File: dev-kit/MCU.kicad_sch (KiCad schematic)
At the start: 34 parts, among them IC107 USBLC6-2P6, IC302 FAN5622SX, IC303 MX25U51245GZ4I00, IC305 NTS0104GU12, M301 NORA-B106, X103 Device, X104 DEBUG, X207 Power, X208 Power, X209 LED Power, X210 Touch Power, X211 IO Power, X302 Display

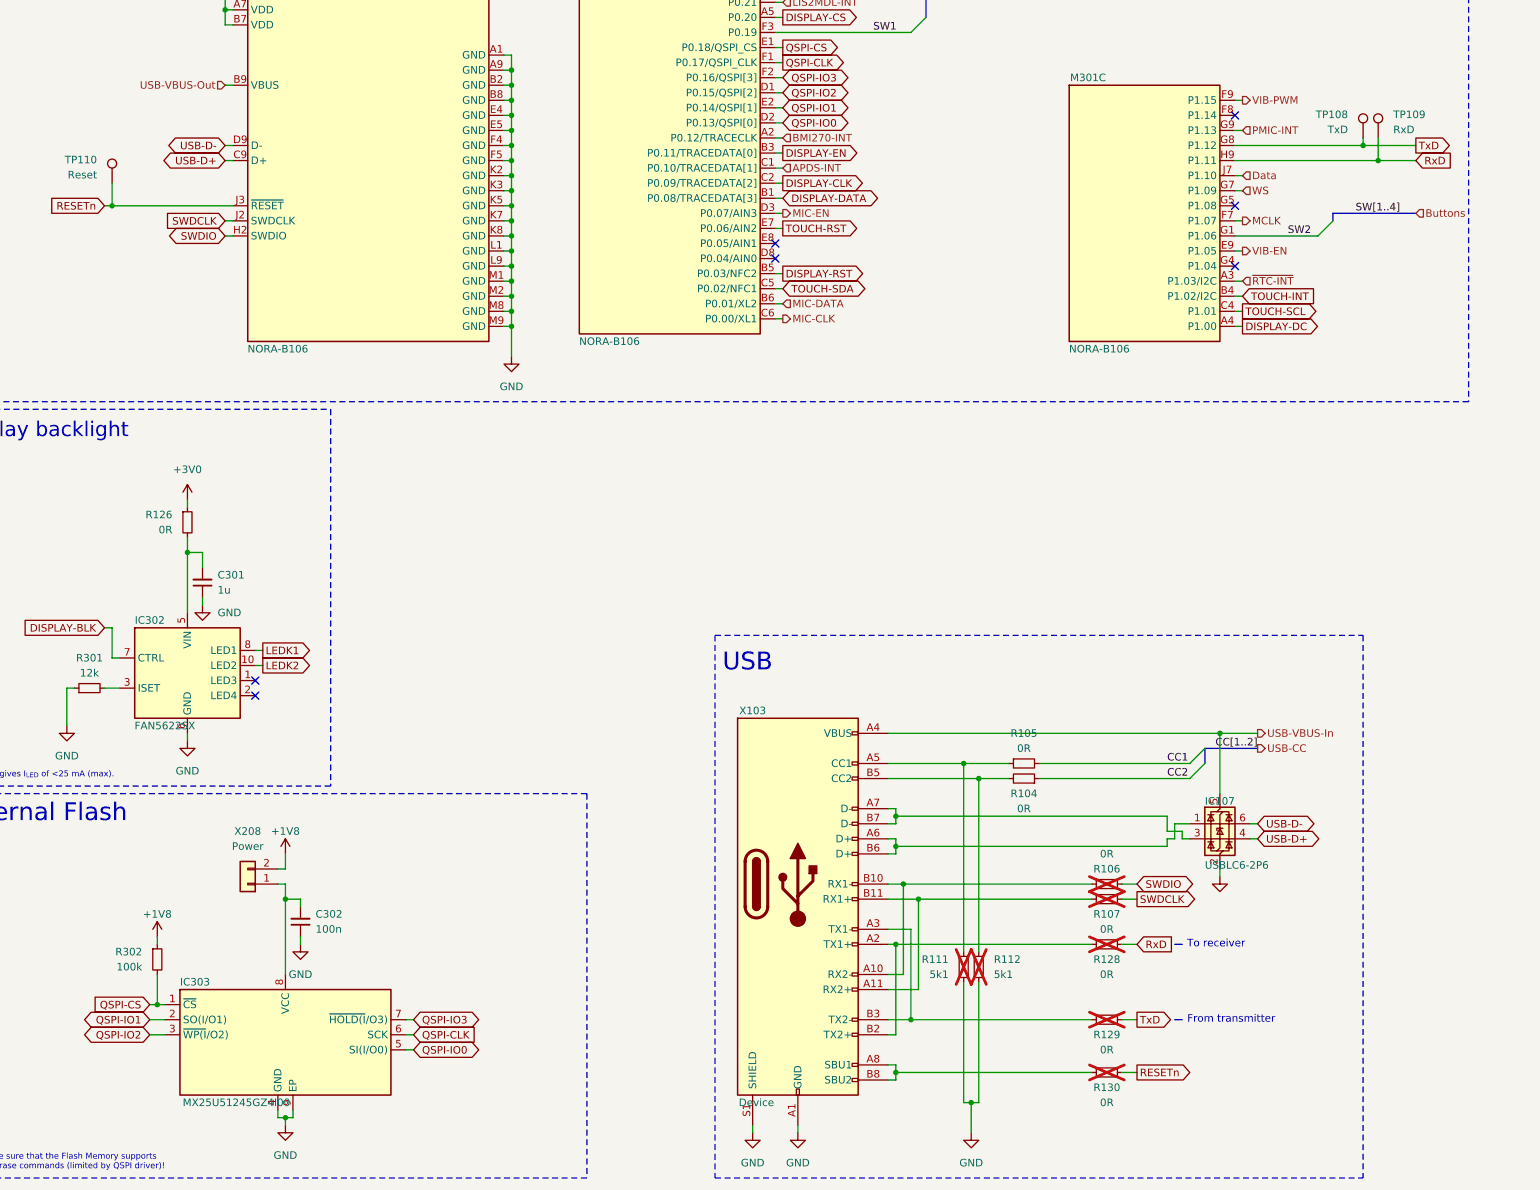
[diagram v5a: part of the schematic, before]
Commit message: PCB: Tweak silkscreen and headers.
- Added silkscreen labels to headers.
- Added function text to buttons.
- Made PCB 5mm wider (left) to make space for display (not sticking out of PCB) and allow more centered
buttons placement.
- Add header for UART pins (good in case we don't have a working dock built) (no mount).
- Changed from TP to header for VBAT for alternative way to connect battery (no mount).
- Added website url on silkscreen.
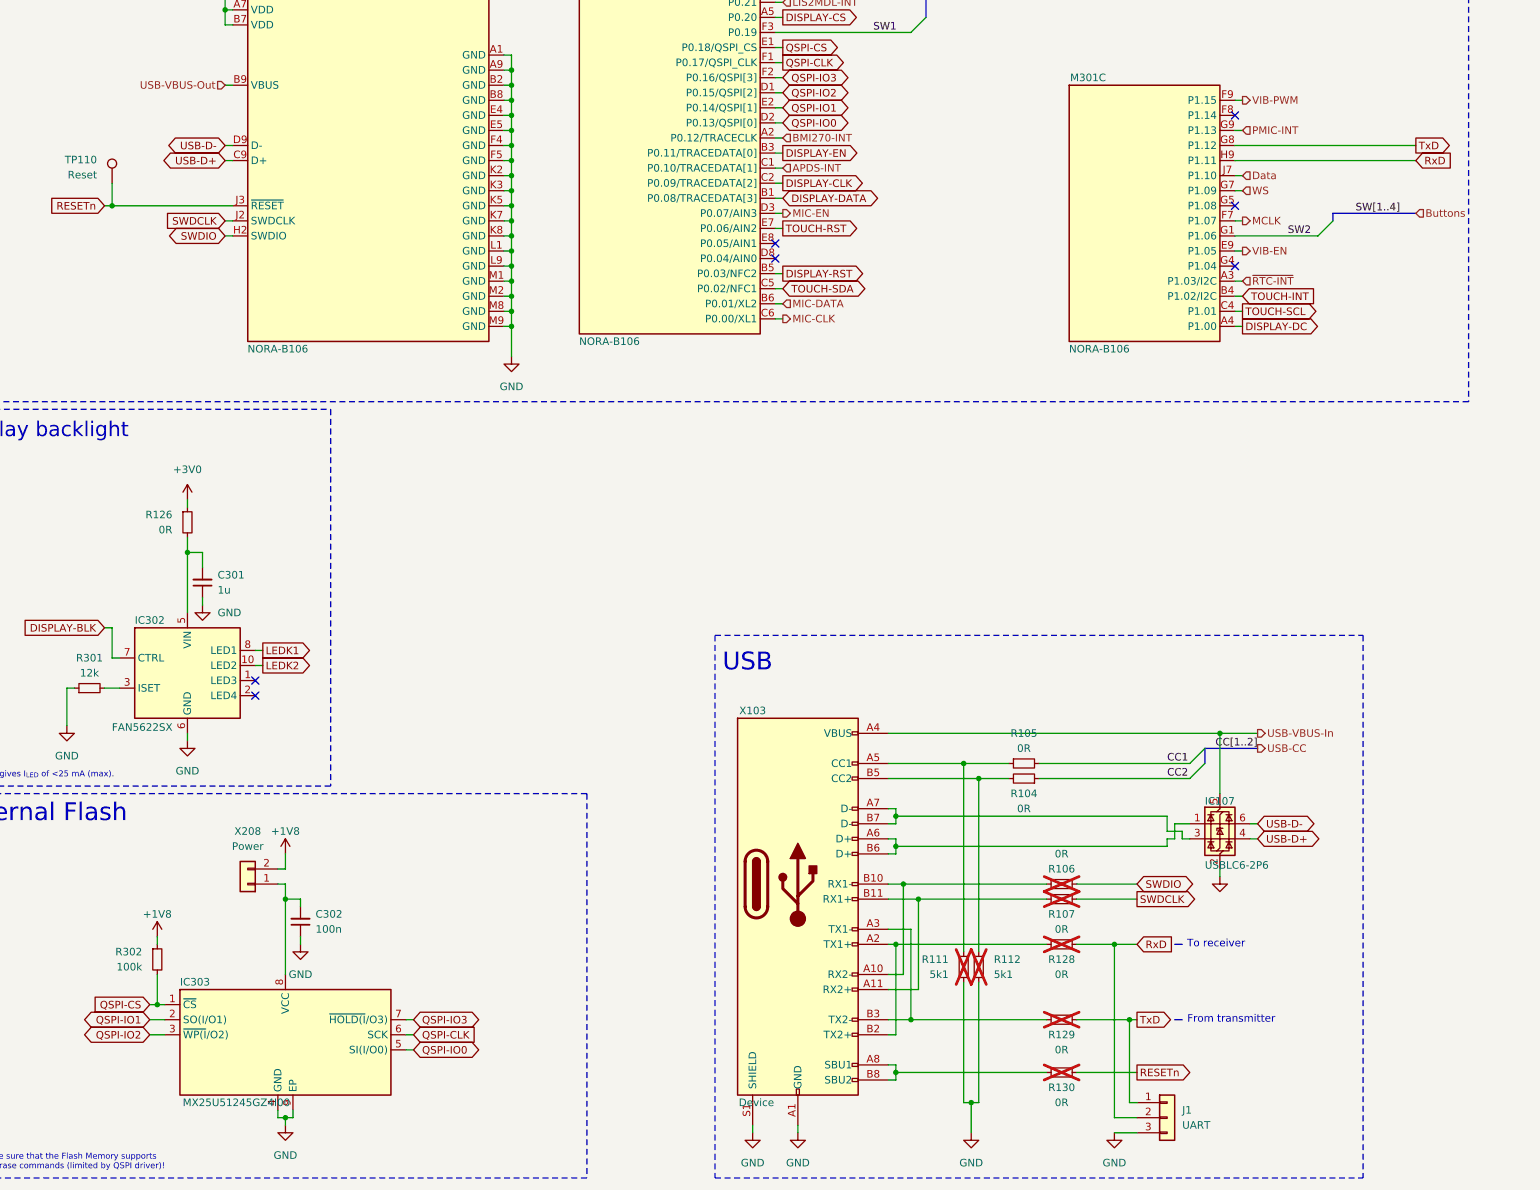
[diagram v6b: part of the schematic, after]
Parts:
- removed TP108: TxD, TestPoint:TestPoint_Pad_D1.0mm, symbol Connector:TestPoint
- removed TP109: RxD, TestPoint:TestPoint_Pad_D1.0mm, symbol Connector:TestPoint
- added J1: UART, Connector_PinHeader_2.54mm:PinHeader_1x03_P2.54mm_Vertical, symbol Connector_Generic:Conn_01x03
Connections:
- net GND: now also J1.3 (Pin_3)
- net RxD: now also J1.2 (Pin_2)
- net TxD: now also J1.1 (Pin_1)
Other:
- moved on the sheet: R106, R107, R128, R129, R130

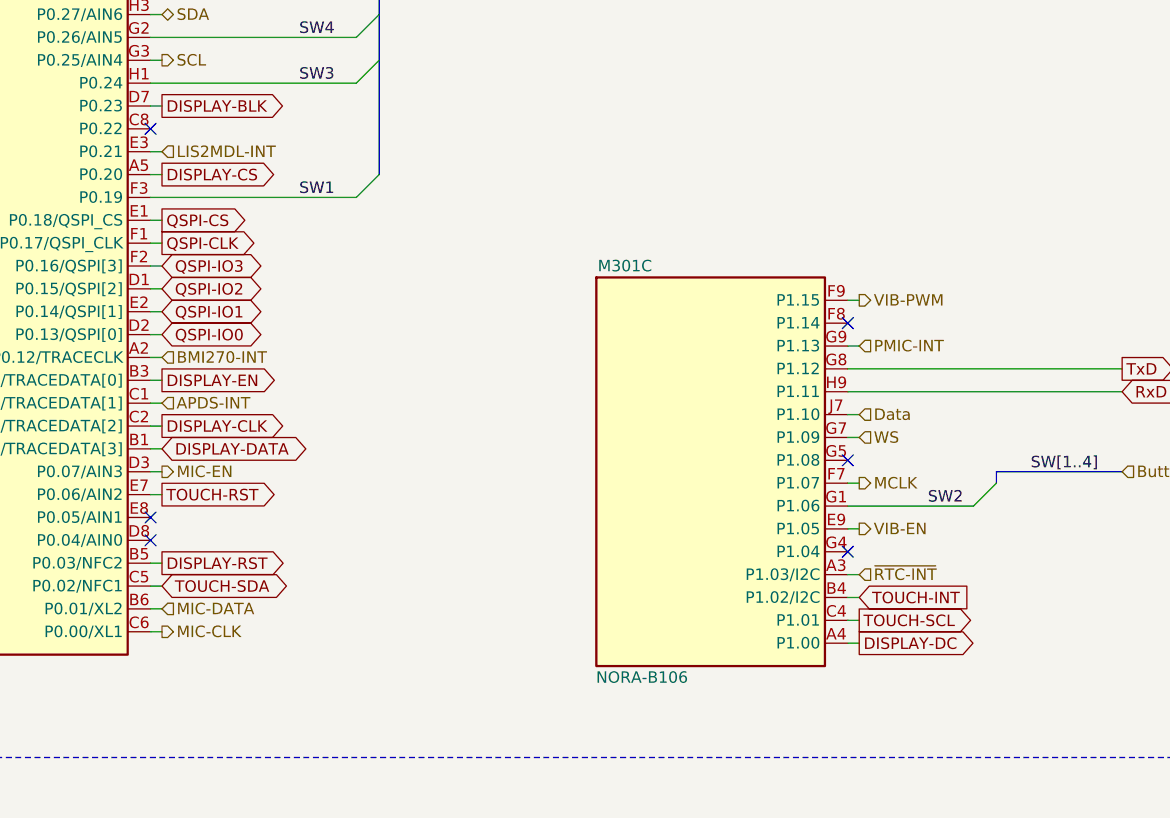
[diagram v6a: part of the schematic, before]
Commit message: Fix wrong display SPI lines
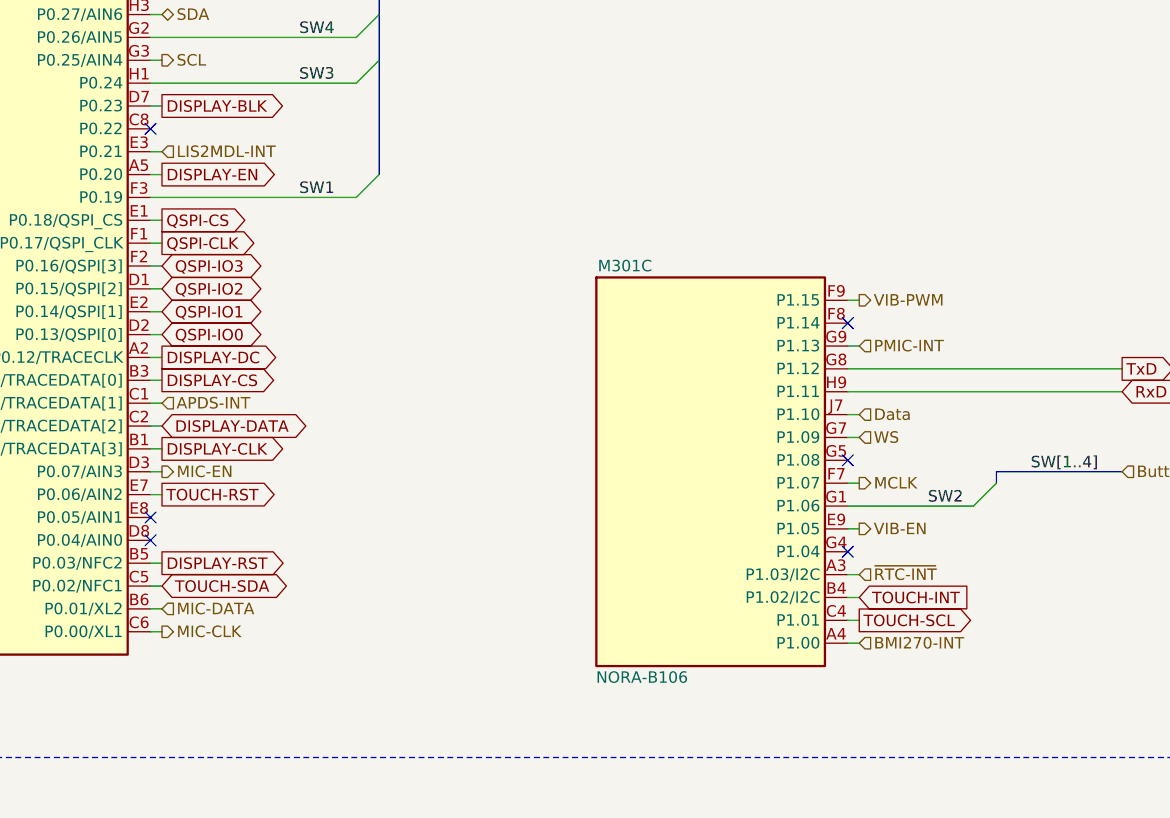
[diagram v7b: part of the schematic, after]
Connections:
- net BMI270-INT: now also M301.A4 (P1.00); no longer M301.A2 (P0.12/TRACECLK)
- net DISPLAY-CLK: now also M301.B1 (P0.08/TRACEDATA[3]); no longer M301.C2 (P0.09/TRACEDATA[2])
- net DISPLAY-CS: now also M301.B3 (P0.11/TRACEDATA[0]); no longer M301.A5 (P0.20)
- net DISPLAY-DATA: now also M301.C2 (P0.09/TRACEDATA[2]); no longer M301.B1 (P0.08/TRACEDATA[3])
- net DISPLAY-DC: now also M301.A2 (P0.12/TRACECLK); no longer M301.A4 (P1.00)
- net DISPLAY-EN: now also M301.A5 (P0.20); no longer M301.B3 (P0.11/TRACEDATA[0])
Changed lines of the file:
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@@
 	(global_label "DISPLAY-DATA"
 		(shape bidirectional)
-		(at 153.67 119.38 0)
-		(fields_autoplaced yes)
-		(effects
-			(font
-				(size 1.27 1.27)
-			)
-			(justify left)
-		)
-		(property "Intersheetrefs" "${INTERSHEET_REFS}"
-			(at 171.3133 119.38 0)
+		(at 153.67 116.84 0)
+		(fields_autoplaced yes)
+		(effects
+			(font
+				(size 1.27 1.27)
+			)
+			(justify left)
+		)
+		(property "Intersheetrefs" "${INTERSHEET_REFS}"
+			(at 171.3133 116.84 0)
 			(effects
 				(font
@@
 	(global_label "DISPLAY-DC"
 		(shape output)
-		(at 231.14 140.97 0)
-		(fields_autoplaced yes)
-		(effects
-			(font
-				(size 1.27 1.27)
-			)
-			(justify left)
-		)
-		(property "Intersheetrefs" "${INTERSHEET_REFS}"
-			(at 245.7972 140.97 0)
+		(at 153.67 109.22 0)
+		(fields_autoplaced yes)
+		(effects
+			(font
+				(size 1.27 1.27)
+			)
+			(justify left)
+		)
+		(property "Intersheetrefs" "${INTERSHEET_REFS}"
+			(at 168.3272 109.22 0)
 			(effects
 				(font
@@
 	(global_label "DISPLAY-CLK"
 		(shape output)
-		(at 153.67 116.84 0)
-		(fields_autoplaced yes)
-		(effects
-			(font
-				(size 1.27 1.27)
-			)
-			(justify left)
-		)
-		(property "Intersheetrefs" "${INTERSHEET_REFS}"
-			(at 169.3553 116.84 0)
+		(at 153.67 119.38 0)
+		(fields_autoplaced yes)
+		(effects
+			(font
+				(size 1.27 1.27)
+			)
+			(justify left)
+		)
+		(property "Intersheetrefs" "${INTERSHEET_REFS}"
+			(at 169.3553 119.38 0)
 			(effects
 				(font
@@
 	(global_label "DISPLAY-CS"
 		(shape output)
+		(at 153.67 111.76 0)
+		(fields_autoplaced yes)
+		(effects
+			(font
+				(size 1.27 1.27)
+			)
+			(justify left)
+		)
+		(property "Intersheetrefs" "${INTERSHEET_REFS}"
+			(at 168.2667 111.76 0)
+			(effects
+				(font
+					(size 1.27 1.27)
+				)
+				(justify left)
+				(hide yes)
+			)
+		)
+	)
+	(global_label "DISPLAY-DC"
+		(shape input)
+		(at 339.09 146.05 180)
+		(fields_autoplaced yes)
+		(effects
+			(font
+				(size 1.27 1.27)
+			)
+			(justify right)
+		)
+		(property "Intersheetrefs" "${INTERSHEET_REFS}"
+			(at 324.4328 146.05 0)
+			(effects
+				(font
+					(size 1.27 1.27)
+				)
+				(justify right)
+				(hide yes)
+			)
+		)
+	)
+	(global_label "RxD"
+		(shape input)
+		(at 213.36 245.11 0)
+		(fields_autoplaced yes)
+		(effects
+			(font
+				(size 1.27 1.27)
+			)
+			(justify left)
+		)
+		(property "Intersheetrefs" "${INTERSHEET_REFS}"
+			(at 219.9133 245.11 0)
+			(effects
+				(font
+					(size 1.27 1.27)
+				)
+				(justify left)
+				(hide yes)
+			)
+		)
+	)
+	(global_label "TxD"
+		(shape output)
+		(at 260.35 110.49 0)
+		(fields_autoplaced yes)
+		(effects
+			(font
+				(size 1.27 1.27)
+			)
+			(justify left)
+		)
+		(property "Intersheetrefs" "${INTERSHEET_REFS}"
+			(at 266.6009 110.49 0)
+			(effects
+				(font
+					(size 1.27 1.27)
+				)
+				(justify left)
+				(hide yes)
+			)
+		)
+	)
+	(global_label "LEDK1"
+		(shape output)
+		(at 66.04 195.58 0)
+		(fields_autoplaced yes)
+		(effects
+			(font
+				(size 1.27 1.27)
+			)
+			(justify left)
+		)
+		(property "Intersheetrefs" "${INTERSHEET_REFS}"
+			(at 74.8724 195.58 0)
+			(effects
+				(font
+					(size 1.27 1.27)
+				)
+				(justify left)
+				(hide yes)
+			)
+		)
+	)
+	(global_label "DISPLAY-EN"
+		(shape output)
 		(at 153.67 88.9 0)
 		(fields_autoplaced yes)
@@
 		)
 	)
-	(global_label "DISPLAY-DC"
-		(shape input)
-		(at 339.09 146.05 180)
-		(fields_autoplaced yes)
-		(effects
-			(font
-				(size 1.27 1.27)
-			)
-			(justify right)
-		)
-		(property "Intersheetrefs" "${INTERSHEET_REFS}"
-			(at 324.4328 146.05 0)
-			(effects
-				(font
-					(size 1.27 1.27)
-				)
-				(justify right)
-				(hide yes)
-			)
-		)
-	)
-	(global_label "RxD"
-		(shape input)
-		(at 213.36 245.11 0)
-		(fields_autoplaced yes)
-		(effects
-			(font
-				(size 1.27 1.27)
-			)
-			(justify left)
-		)
-		(property "Intersheetrefs" "${INTERSHEET_REFS}"
-			(at 219.9133 245.11 0)
-			(effects
-				(font
-					(size 1.27 1.27)
-				)
-				(justify left)
-				(hide yes)
-			)
-		)
-	)
-	(global_label "TxD"
-		(shape output)
-		(at 260.35 110.49 0)
-		(fields_autoplaced yes)
-		(effects
-			(font
-				(size 1.27 1.27)
-			)
-			(justify left)
-		)
-		(property "Intersheetrefs" "${INTERSHEET_REFS}"
-			(at 266.6009 110.49 0)
-			(effects
-				(font
-					(size 1.27 1.27)
-				)
-				(justify left)
-				(hide yes)
-			)
-		)
-	)
-	(global_label "LEDK1"
-		(shape output)
-		(at 66.04 195.58 0)
-		(fields_autoplaced yes)
-		(effects
-			(font
-				(size 1.27 1.27)
-			)
-			(justify left)
-		)
-		(property "Intersheetrefs" "${INTERSHEET_REFS}"
-			(at 74.8724 195.58 0)
-			(effects
-				(font
-					(size 1.27 1.27)
-				)
-				(justify left)
+	(global_label "RESETn"
+		(shape output)
+		(at 396.24 219.71 0)
+		(fields_autoplaced yes)
+		(effects
+			(font
+				(size 1.27 1.27)
+			)
+			(justify left)
+		)
+		(property "Intersheetrefs" "${INTERSHEET_REFS}"
+			(at 406.1193 219.71 0)
+			(effects
+				(font
+					(size 1.27 1.27)
+				)
+				(justify left)
+				(hide yes)
+			)
+		)
+	)
+	(global_label "DISPLAY-RST"
+		(shape input)
+		(at 339.09 134.62 180)
+		(fields_autoplaced yes)
+		(effects
+			(font
+				(size 1.27 1.27)
+			)
+			(justify right)
+		)
+		(property "Intersheetrefs" "${INTERSHEET_REFS}"
+			(at 323.5257 134.62 0)
+			(effects
+				(font
+					(size 1.27 1.27)
+				)
+				(justify right)
 				(hide yes)
 			)
@@
 	)
 	(global_label "DISPLAY-EN"
-		(shape output)
-		(at 153.67 111.76 0)
-		(fields_autoplaced yes)
-		(effects
-			(font
-				(size 1.27 1.27)
-			)
-			(justify left)
-		)
-		(property "Intersheetrefs" "${INTERSHEET_REFS}"
-			(at 168.2667 111.76 0)
-			(effects
-				(font
-					(size 1.27 1.27)
-				)
-				(justify left)
-				(hide yes)
-			)
-		)
-	)
-	(global_label "RESETn"
-		(shape output)
-		(at 396.24 219.71 0)
-		(fields_autoplaced yes)
-		(effects
-			(font
-				(size 1.27 1.27)
-			)
-			(justify left)
-		)
-		(property "Intersheetrefs" "${INTERSHEET_REFS}"
-			(at 406.1193 219.71 0)
-			(effects
-				(font
-					(size 1.27 1.27)
-				)
-				(justify left)
-				(hide yes)
-			)
-		)
-	)
-	(global_label "DISPLAY-RST"
-		(shape input)
-		(at 339.09 134.62 180)
-		(fields_autoplaced yes)
-		(effects
-			(font
-				(size 1.27 1.27)
-			)
-			(justify right)
-		)
-		(property "Intersheetrefs" "${INTERSHEET_REFS}"
-			(at 323.5257 134.62 0)
-			(effects
-				(font
-					(size 1.27 1.27)
-				)
-				(justify right)
-				(hide yes)
-			)
-		)
-	)
-	(global_label "DISPLAY-EN"
 		(shape input)
 		(at 337.82 68.58 180)
@@
 	(hierarchical_label "BMI270-INT"
 		(shape input)
-		(at 153.67 109.22 0)
-		(effects
-			(font
+		(at 231.14 140.97 0)
+		(effects
+			(font

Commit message: Changes from Jacob
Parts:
- added X310: GPIO, Connector_PinHeader_2.54mm:PinHeader_1x06_P2.54mm_Vertical_SMD_Pin1Left, symbol Connector_Generic:Conn_01x06
- R304: renamed from R111; manf (none) -> Bourns; manf# (none) -> CR0402-FX-5101GLF; mouser# (none) -> 652-CR0402-FX-5101GLF; now left out of the parts list
- R305: renamed from R112; manf (none) -> Bourns; manf# (none) -> CR0402-FX-5101GLF; mouser# (none) -> 652-CR0402-FX-5101GLF; now left out of the parts list
- X304: renamed from J1; manf (none) -> Amphenol FCI; manf# (none) -> 10129378-936001BLF; mouser# (none) -> 649-1012937893601BLF
- X309: renamed from X104; now fitted; now in the parts list
- renumbered C304 to C303, C305 to C304, IC302 to IC301, IC303 to IC302, IC107 to IC303, IC305 to IC304, R126 to R303, R105 to R306, R104 to R307, R106 to R308, R107 to R309, R128 to R310, R129 to R311, R130 to R312, R117 to R313, R118 to R314, TP110 to TP301, X207 to X301, X208 to X302, X103 to X303, X211 to X305, X302 to X306, X210 to X307, X209 to X308
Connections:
- net +1V8: now also X310.6 (Pin_6)
- net GND: now also X310.5 (Pin_5)
- net USB-D+: now also IC303.6 (I/O1); no longer IC303.4 (I/O2)
- net USB-D-: now also IC303.4 (I/O2); no longer IC303.6 (I/O1)
- net at M301.C8 (P0.22): now also X310.1 (Pin_1)
- net at M301.D8 (P0.04/AIN0): now also X310.3 (Pin_3)
- net at M301.E8 (P0.05/AIN1): now also X310.2 (Pin_2)
- net at M301.F8 (P1.14): now also X310.4 (Pin_4)
- no-connect marks 16 -> 12
